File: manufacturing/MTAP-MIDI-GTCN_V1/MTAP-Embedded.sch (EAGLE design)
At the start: 59 parts, among them IC1 ESP32-WROOM-32UE-N8, IC2 AMS1117-3.3, IC3 TPS60402DBVT, J1 629105150521, X2 22-23-2021

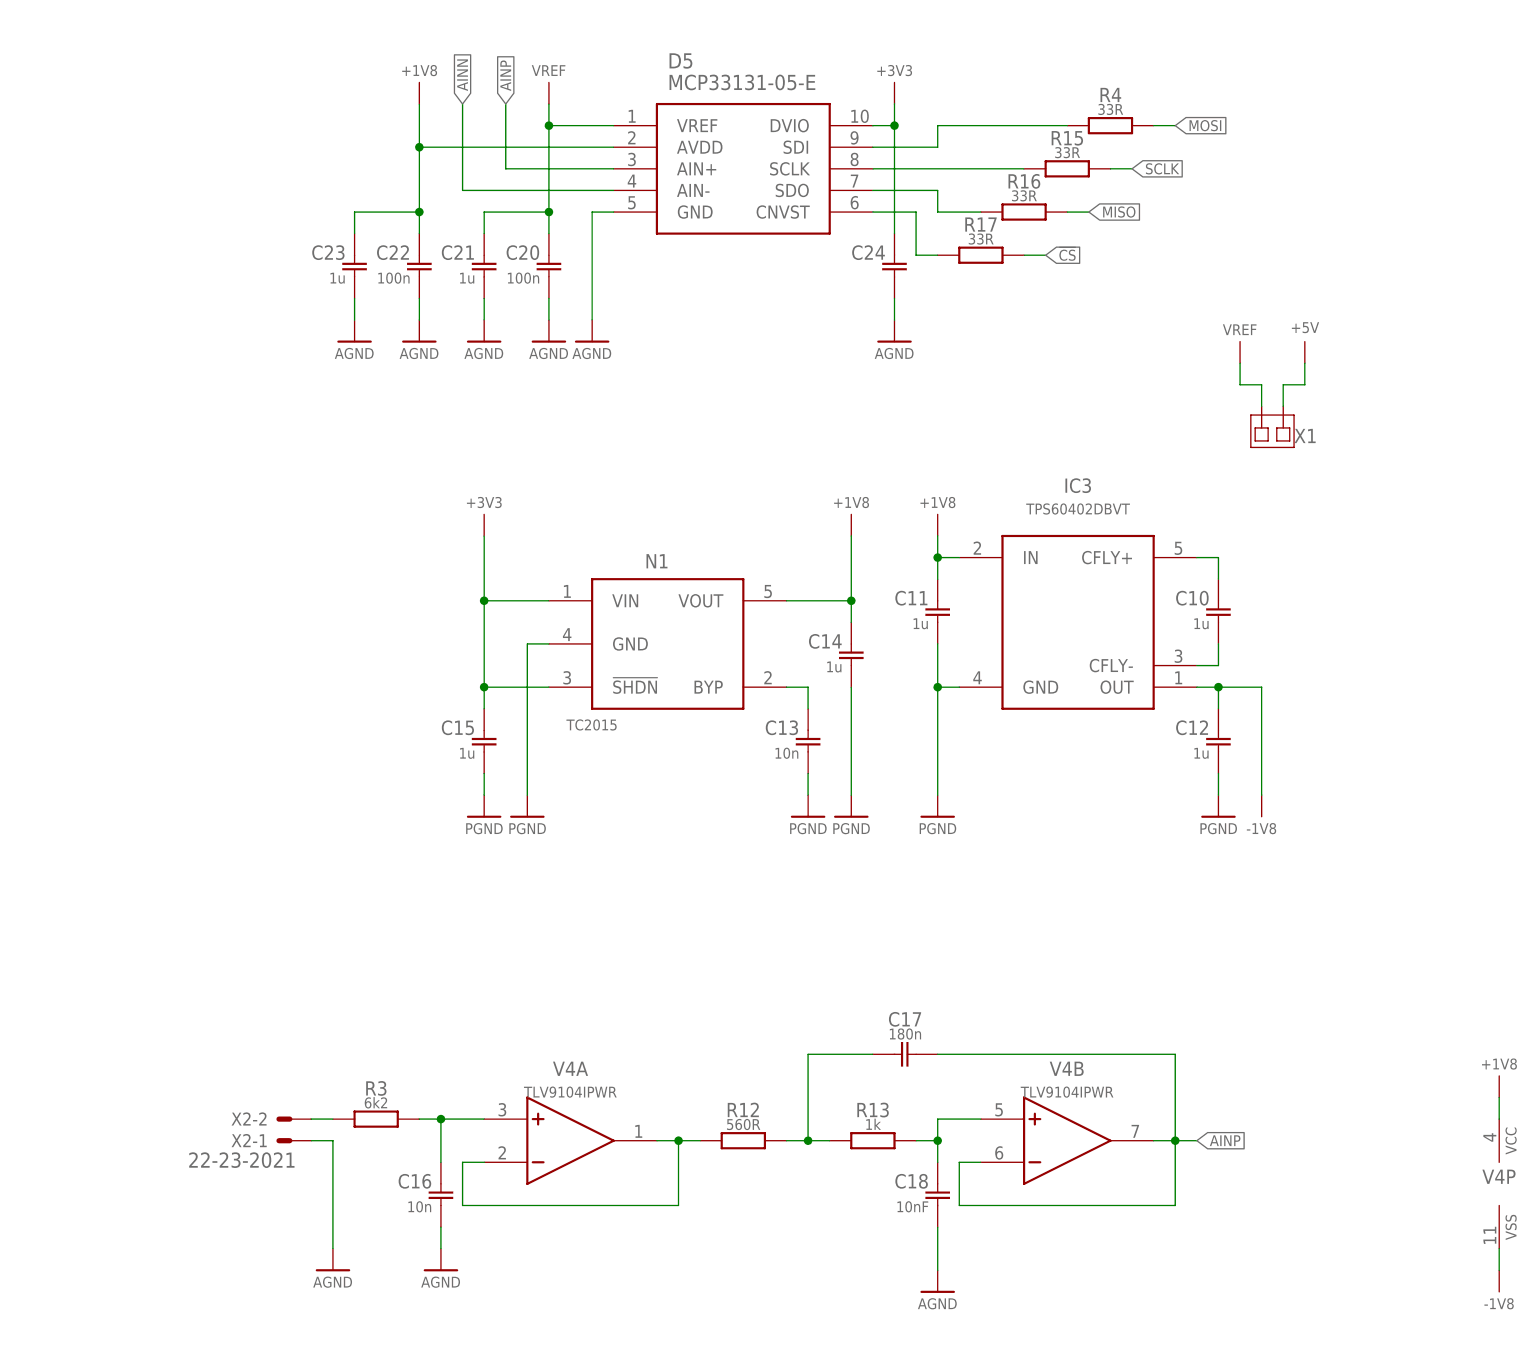
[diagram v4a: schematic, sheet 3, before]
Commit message: upd schematic to fix adc problem
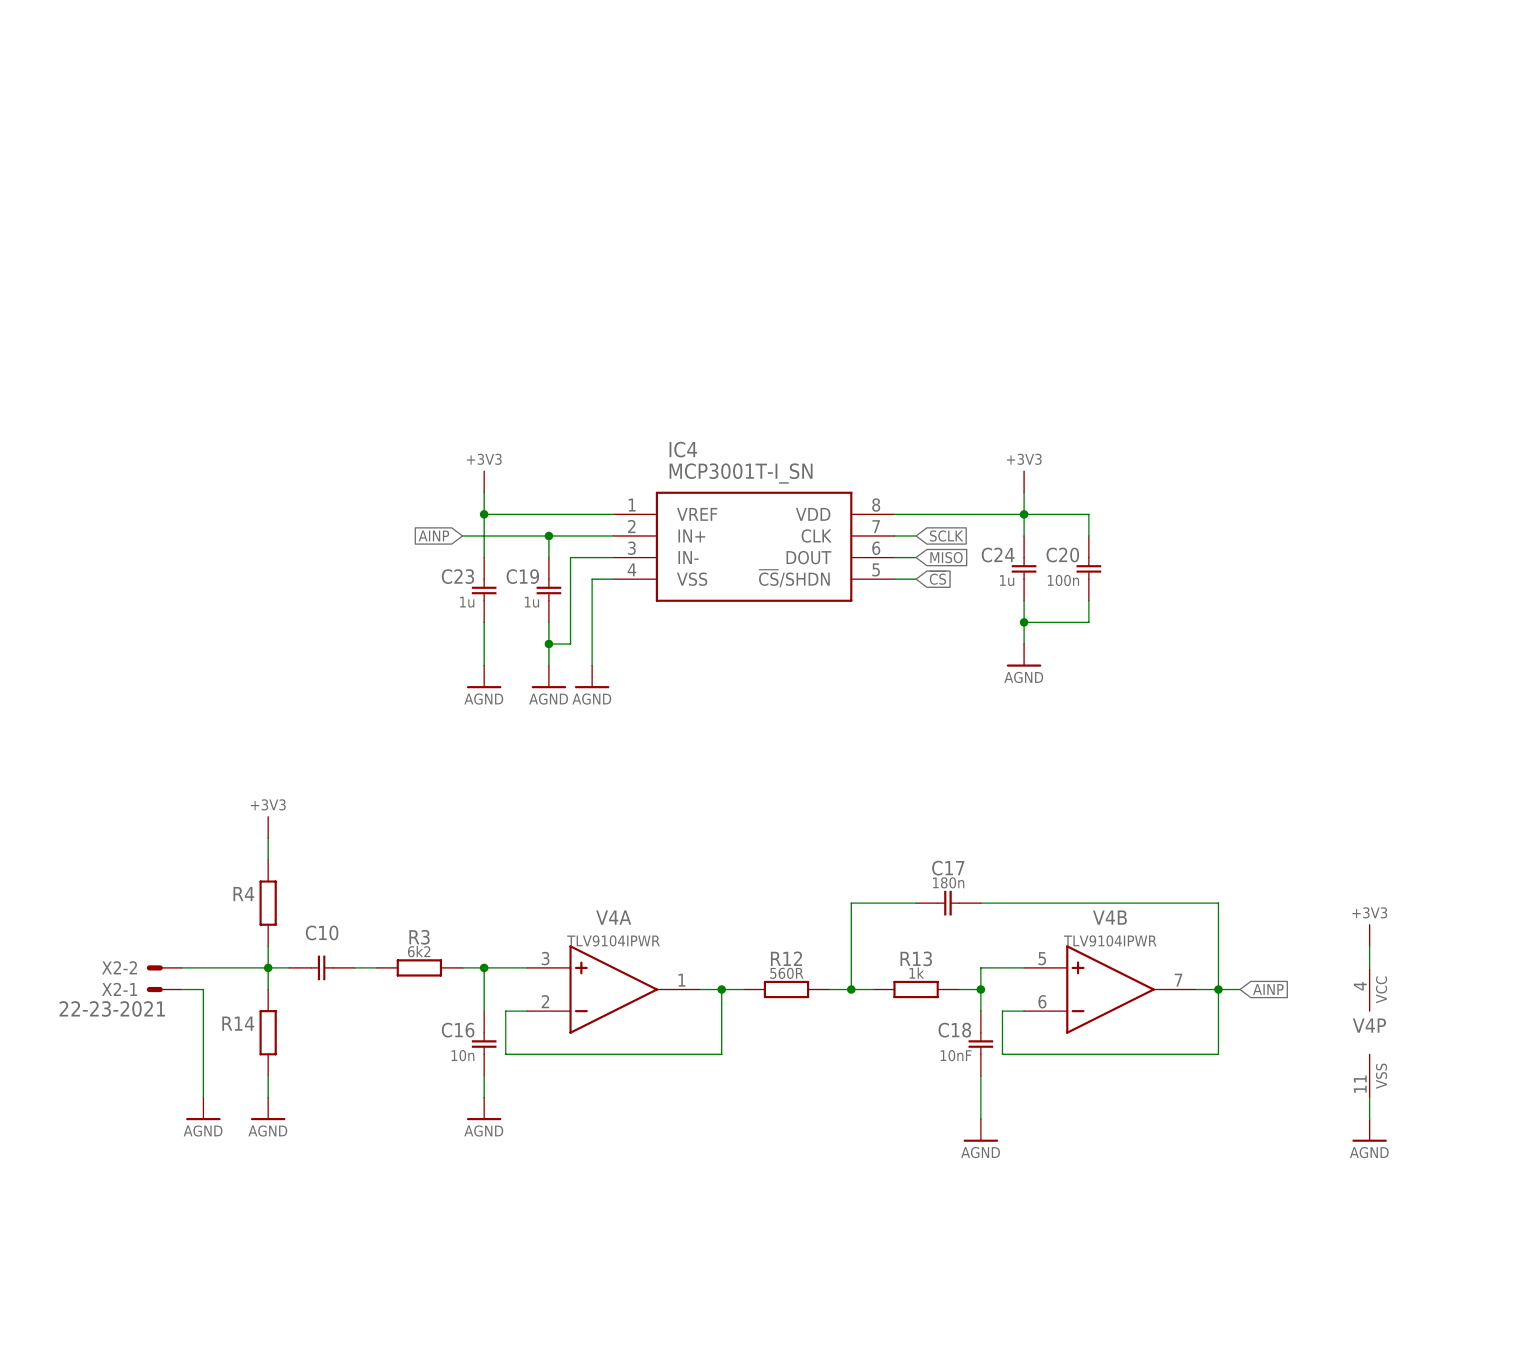
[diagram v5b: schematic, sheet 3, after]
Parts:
- removed C11, C12, C14, C15, C21: 1u, rcl_GruS:C-EUC0805
- removed C13: 10n, rcl_GruS:C-EUC0805
- removed C22: 100n, rcl_GruS:C-EUC0805
- removed D5: MCP33131-05-E, adc-dac_GruS:MCP33131-05-E
- removed IC3: TPS60402DBVT, vreg_GruS:TPS60402DBVT
- removed N1: TC2015, vreg_GruS:TC2015
- removed R15, R16, R17: 33R, rcl_GruS:R-EU_R0805
- removed X1: (no value), con_GruS:JUMPSMD1FACH-1SHORT
- added C19: 1u, rcl_GruS:C-EUC0805
- added IC4: MCP3001T-I_SN, adc-dac_GruS:MCP3001T-I_SN
- added R14: (no value), rcl_GruS:R-EUSR0805
- C10: value 1u -> (none); device rcl_GruS:C-EUC0805 -> rcl_GruS:C-EULC0805
- C24: value (none) -> 1u
- R4: value 33R -> (none); device rcl_GruS:R-EU_R0805 -> rcl_GruS:R-EUSR0805
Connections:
- removed net +1V8: C11.1, C14.1, C22.1, C23.1, D5.AVDD, IC3.IN, N1.VOUT, V4P.VCC
- removed net -1V8: C12.1, IC3.OUT, V4P.VSS
- removed net AINN: D5.AIN-
- removed net MOSI: R4.2
- removed net N$10: C13.1, N1.BYP
- removed net N$11: D5.SDO, R16.1
- removed net N$14: D5.SCLK, R15.1
- removed net N$18: C10.1, IC3.CFLY+
- removed net N$19: D5.SDI, R4.1
- removed net N$5: D5.CNVST, R17.1
- removed net VREF: C20.1, C21.1, D5.VREF, X1.2
- net !CS: now also IC4.!CS!/SHDN; no longer R17.2
- net +3V3: now also C20.1, C23.1, IC4.VDD, IC4.VREF, R4.2, V4P.VCC; no longer C15.1, D5.DVIO, N1.!SHDN, N1.VIN
- net +5V: no longer X1.1
- net AGND: now also C19.2, IC4.IN-, IC4.VSS, R14.1, V4P.VSS; no longer C21.2, C22.2, D5.GND
- net AINP: now also C19.1, IC4.IN+; no longer D5.AIN+
- net MISO: now also IC4.DOUT; no longer R16.2
- net N$17: now also R14.2, R4.1, X2-2.S; no longer IC3.CFLY-
- net N$8: now also C10.1; no longer X2-2.S
- net PGND: no longer C11.2, C12.2, C13.2, C14.2, C15.2, IC3.GND, N1.GND
- net SCLK: now also IC4.CLK; no longer R15.2
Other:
- moved on the sheet: C10, C16, C17, C18, C20, C23, C24, R12, R13, R3, R4, V4A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

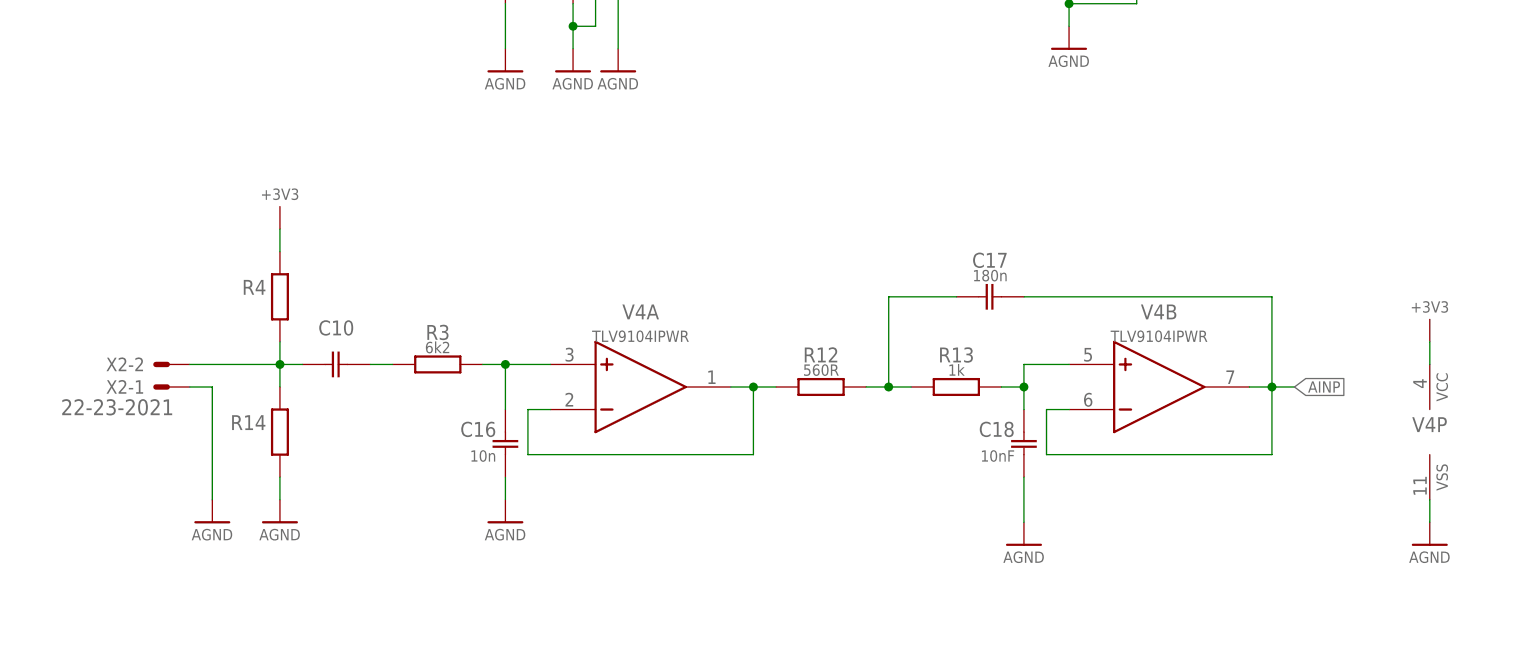
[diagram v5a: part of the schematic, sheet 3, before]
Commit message: update analogue process chain onboard
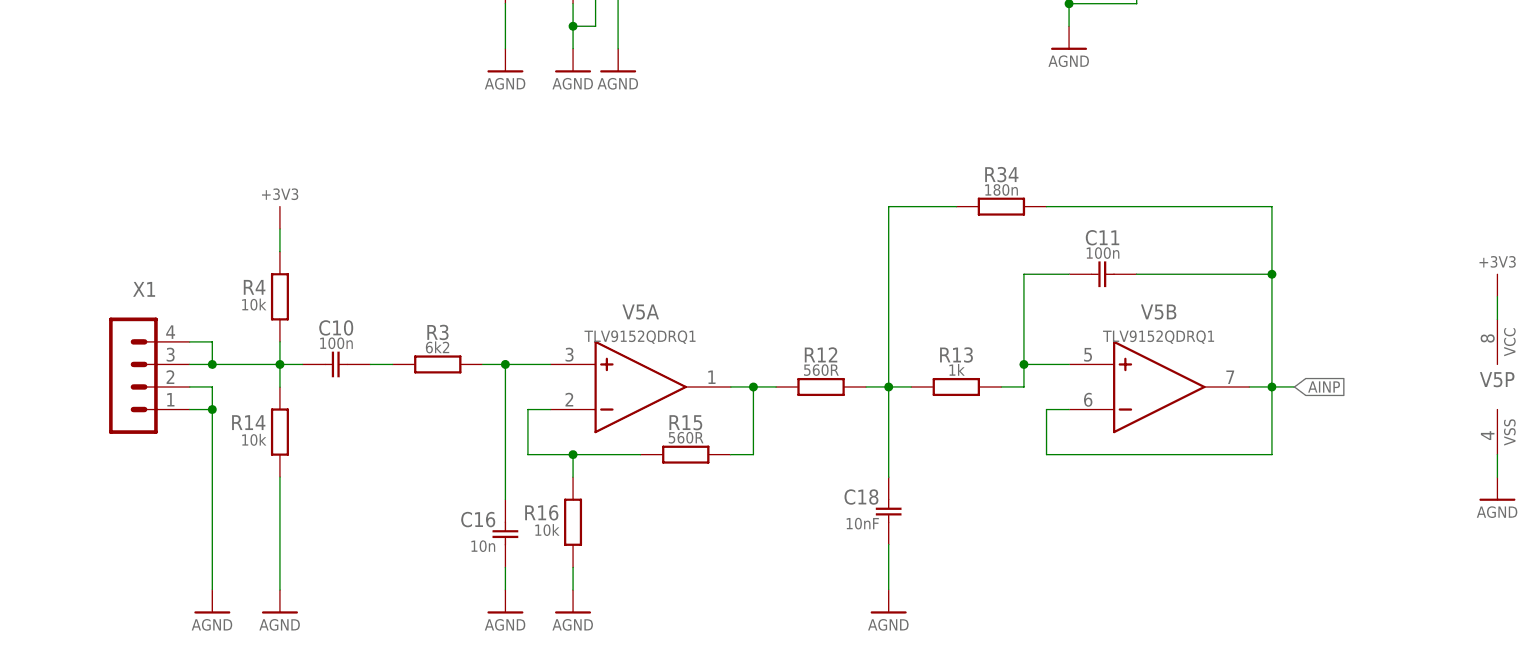
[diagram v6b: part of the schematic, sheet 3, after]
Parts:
- removed C17: 180n, rcl_GruS:C-EULC0805
- removed V4: TLV9104IPWR, opv_GruS:TLV9104IPWR
- removed X2: 22-23-2021, con-molex:22-23-2021
- added C11: 100n, rcl_GruS:C-EULC0805
- added R15: 560R, rcl_GruS:R-EU_R0805
- added R16: 10k, rcl_GruS:R-EUSR0805
- added R34: 180n, rcl_GruS:R-EU_R0805
- added V5: TLV9152QDRQ1, opv_GruS:TLV9152QDRQ1
- added X1: (no value), con-lstb:MA04-1
- C10: value (none) -> 100n
- R14, R4: value (none) -> 10k
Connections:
- new net N$5: R15.1, R16.2, V5A.N
- net +3V3: now also V5P.VCC; no longer V4P.VCC
- net AGND: now also R16.1, V5P.VSS, X1.1, X1.2; no longer V4P.VSS, X2-1.S
- net AINP: now also C11.1, R34.1, V5B.N, V5B.O; no longer C17.1, V4B.N, V4B.O
- net N$12: now also C11.2, V5B.P; no longer C18.1, V4B.P
- net N$17: now also X1.3, X1.4; no longer X2-2.S
- net N$6: now also R15.2, V5A.O; no longer V4A.N, V4A.O
- net N$7: now also V5A.P; no longer V4A.P
- net N$9: now also C18.1, R34.2; no longer C17.2
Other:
- moved on the sheet: C16, C18

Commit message: finished PCB
issues with filter circuit only works wit dual supply. negative voltage may be needed
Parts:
- removed C19, C23, C24: 1u, rcl_GruS:C-EUC0805
- removed C20: 100n, rcl_GruS:C-EUC0805
- removed IC1: ESP32-WROOM-32UE-N8, modul_GruS:ESP32-WROOM-32UE-N8
- removed IC2: AMS1117-3.3, vreg_GruS:AMS1117-3.3
- removed IC4: MCP3001T-I_SN, adc-dac_GruS:MCP3001T-I_SN
- removed R34: 180n, rcl_GruS:R-EU_R0805
- removed S4: (no value), switch_GruS:452404020202
- removed V5: TLV9152QDRQ1, opv_GruS:TLV9152QDRQ1
- added C12, C13: 1u, rcl_GruS:C-EUC0805
- added C14: 10nF, rcl_GruS:C-EULC0805
- added C15: 100n, rcl_GruS:C-EULC0805
- added C17: 10n, rcl_GruS:C-EUC0805
- added D5: LESD5D5.0CT1G, diode_GruS:LESD5D5.0CT1G
- added D6: MCP3201-CI_SN, adc-dac_GruS:MCP3201-CI_SN
- added L1: 10u, rcl_GruS:L-EU-POERL3216C
- added N1: AMS1117-3.3, vreg_GruS:AMS1117-3.3
- added S3: (no value), switch_GruS:452404020202
- added V4: TLV9152QDRQ1, opv_GruS:TLV9152QDRQ1
- added X2: 0R, con_GruS:JUMPSMD1FACH-1SHORT
- added X3: (no value), con-lstb:MA04-1
- C10: value 100n -> 1u; device rcl_GruS:C-EULC0805 -> rcl_GruS:C-EUC0805
- C11: device rcl_GruS:C-EULC0805 -> rcl_GruS:C-EUC0805
- C16: value 10n -> 680n
- C18: value 10nF -> 100n
- C2: value 22u/10V -> 100n/50V
- C4: value 22u/10V -> 4u7
- C5: value 100n/50V -> 100n
- C6, C7: value 100n -> 22u/10V; device rcl_GruS:C-EULC0805 -> rcl_GruS:C-EUC0805
- C8, C9: value (none) -> 100n; device rcl_GruS:C-EUC0805 -> rcl_GruS:C-EULC0805
- D1: value CP2102N-A01-GQFN28 -> ESP32-WROOM-32UE-N8; device ic_GruS:CP2102N-A01-GQFN28 -> modul_GruS:ESP32-WROOM-32UE-N8
- D2: value LESD5D5.0CT1G -> CP2102N-A01-GQFN28; device diode_GruS:LESD5D5.0CT1G -> ic_GruS:CP2102N-A01-GQFN28
- R1: value 2k -> 10k
- R11: value 0R -> 12k; device con_GruS:JUMPSMD1FACH-1SHORT -> rcl_GruS:R-EU_R0805
- R12: value 560R -> 430R
- R13: value 1k -> 430R
- R15: value 560R -> 5k1
- R16: value 10k -> 2k4
- R2: device rcl_GruS:R-EUSR0805 -> rcl_GruS:R-EU_R0805
- R3: value 6k2 -> 2k; device rcl_GruS:R-EU_R0805 -> rcl_GruS:R-EUSR0805
- R4: value 10k -> 22k1
- R6: device rcl_GruS:R-EU_R0805 -> rcl_GruS:R-EUSR0805
- R8: value 22k1 -> 2k; device rcl_GruS:R-EU_R0805 -> rcl_GruS:R-EUSR0805
- R9: value 2k -> 1k3
- X1: value (none) -> 0R; device con-lstb:MA04-1 -> con_GruS:JUMPSMD1FACH-1SHORT
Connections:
- removed net !CS: IC4.!CS!/SHDN
- removed net BCLK: IC1.IO22
- removed net CTS: D1.CTS
- removed net DCD: D1.DCD
- removed net DSR: D1.DSR
- removed net FSYNC: IC1.IO23
- removed net FTM0: IC1.IO17
- removed net GPIO12: IC1.IO12
- removed net GPIO13: IC1.IO13
- removed net GPIO14: IC1.IO14
- removed net GPIO15: IC1.IO15
- removed net GPIO16: IC1.IO16
- removed net GPIO2: IC1.IO2
- removed net GPIO25: IC1.IO25
- removed net GPIO32: IC1.IO32
- removed net GPIO33: IC1.IO33
- removed net GPIO34: IC1.IO34
- removed net GPIO35: IC1.IO35
- removed net GPIO4: IC1.IO4
- removed net MD0: IC1.IO18
- removed net MD1: IC1.IO19
- removed net MISO: IC4.DOUT
- removed net MSZ: IC1.IO5
- removed net RI: D1.RI/CLK
- removed net SCLK: IC4.CLK
- removed net SDATA: IC1.IO21
- new net AVDD: C10.1, C11.1, C12.1, C18.1, D6.VDD, D6.VREF, L1.2, R10.2, V4P.VCC
- new net VSPIQ_MISO: D1.IO19, D6.DOUT
- new net VSPI_!CS: D1.IO5, D6.!CS!/SHDN
- new net VSPI_CLK: D1.IO18, D6.CLK
- net +3V3: now also C2.1, C5.1, C7.1, D1.3V3, D2.VDD, D2.VREGIN, L1.1, N1.VOUT, R1.2, R3.1; no longer C20.1, C23.1, C24.1, C3.1, C8.1, C9.1, D1.VDD, D1.VREGIN, IC1.3V3, IC2.VOUT, IC4.VDD, IC4.VREF, R2.2, R4.2, R9.1, V5P.VCC
- net +5V: now also C6.1, N1.VIN, R8.2; no longer C2.1, IC2.VIN, R1.2
- net AGND: now also C10.2, C11.2, C12.2, C13.2, C17.2, D6.IN-, D6.VSS, V4B.P, V4P.VSS, X2.2, X3.1, X3.2; no longer C19.2, C20.2, C23.2, C24.2, IC4.IN-, IC4.VSS, V5P.VSS, X1.1, X1.2
- net AINP: now also C13.1, C14.1, D6.IN+, R9.1, V4B.O; no longer C11.1, C19.1, IC4.IN+, R34.1, V5B.N, V5B.O
- net DTR: now also D2.DTR, R2.1; no longer D1.DTR, R5.1
- net EN: now also C3.1, C9.1, D1.EN, R1.1; no longer C5.1, C7.1, IC1.EN, R2.1
- net GND: now also C1.2, C2.2, D1.GND_1, D1.GND_10, D1.GND_11, D1.GND_12, D1.GND_2, D1.GND_3, D1.GND_4, D1.GND_5, D1.GND_6, D1.GND_7, D1.GND_8, D1.GND_9, D2.GND, X1.2; no longer C4.2, C5.2, D1.GND, IC1.GND_1, IC1.GND_10, IC1.GND_11, IC1.GND_12, IC1.GND_2, IC1.GND_3, IC1.GND_4, IC1.GND_5, IC1.GND_6, IC1.GND_7, IC1.GND_8, IC1.GND_9, R11.2
- net GPIO0: now also C8.1, D1.IO0; no longer C6.1, IC1.IO0
- net N$1: now also R8.1; no longer R1.1
- net N$12: now also C14.2, V4B.N; no longer C11.2, V5B.P
- net N$15: now also R2.2; no longer R5.2
- net N$16: now also R5.2; no longer R6.2
- net N$17: now also C15.2, X3.3, X3.4; no longer C10.2, R14.2, R4.1, X1.3, X1.4
- net N$2: now also D2.VBUS, R4.2; no longer D1.VBUS, R8.2
- net N$3: now also D2.SUSPENDB, R6.2; no longer D1.SUSPENDB, R10.2
- net N$4: now also D2.RSTB, R3.2; no longer D1.RSTB, R9.2
- net N$5: now also V4A.N; no longer V5A.N
- net N$6: now also V4A.O; no longer V5A.O
- net N$7: now also C17.1, R11.2, V4A.P; no longer C16.1, R3.2, V5A.P
- net N$8: now also C15.1, R10.1, R11.1, R14.2; no longer C10.1, R3.1
- net N$9: now also C16.1, R9.2; no longer C18.1, R34.2
- net PGND: now also C4.2, C5.2, D2.THERMAL_PAD, D5.2, N1.GND/ADJ, R6.1, X1.1, X2.1; no longer C1.2, C2.2, D1.THERMAL_PAD, D2.2, IC2.GND/ADJ, R10.1, R11.1
- net RTS: now also D2.RTS, R5.1; no longer D1.RTS, R6.1
- net RXD: now also D2.RXD, S3.COM; no longer D1.RXD, S4.COM
- net RXD0: now also D1.RXD0, S3.4; no longer IC1.RXD0, S4.4
- net RXD1: now also D1.IO27, S3.6; no longer IC1.IO27, S4.6
- net TXD: now also D2.TXD, S3.COM1; no longer D1.TXD, S4.COM1
- net TXD0: now also D1.TXD0, S3.1; no longer IC1.TXD0, S4.1
- net TXD1: now also D1.IO26, S3.3; no longer IC1.IO26, S4.3
- net USB_DN: now also D2.D-, D5.1; no longer D1.D-, D4.1
- net USB_DP: now also D2.D+, D4.1; no longer D1.D+, D3.1
- net VBUS: now also D3.1, R4.1; no longer D2.1, R8.1
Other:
- note added: "5V -> 3.3V Low Dropout Regulator"
- note added: "Analogue Voltage Supply and Reference"
- note added: "Boot Mode and Reset button & UART0/1 Slider Switch"
- note added: "E7 Filter (2637.02Hz) 10V/V Gain Multiple Feedback Single Supply"
- note added: "ESP32 Processor"
- note added: "Low Pass Filter"
- note added: "Post Filter 12 Bit ADC with SPI Interface"
- note added: "USB Bridge"
